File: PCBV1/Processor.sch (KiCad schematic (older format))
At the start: 51 parts, among them SW2 SW_DIP_x02, U1 MCIMX6Y2CVM08AB, Y2 ECS.32712.512, Y3 ECS2401823BJTM

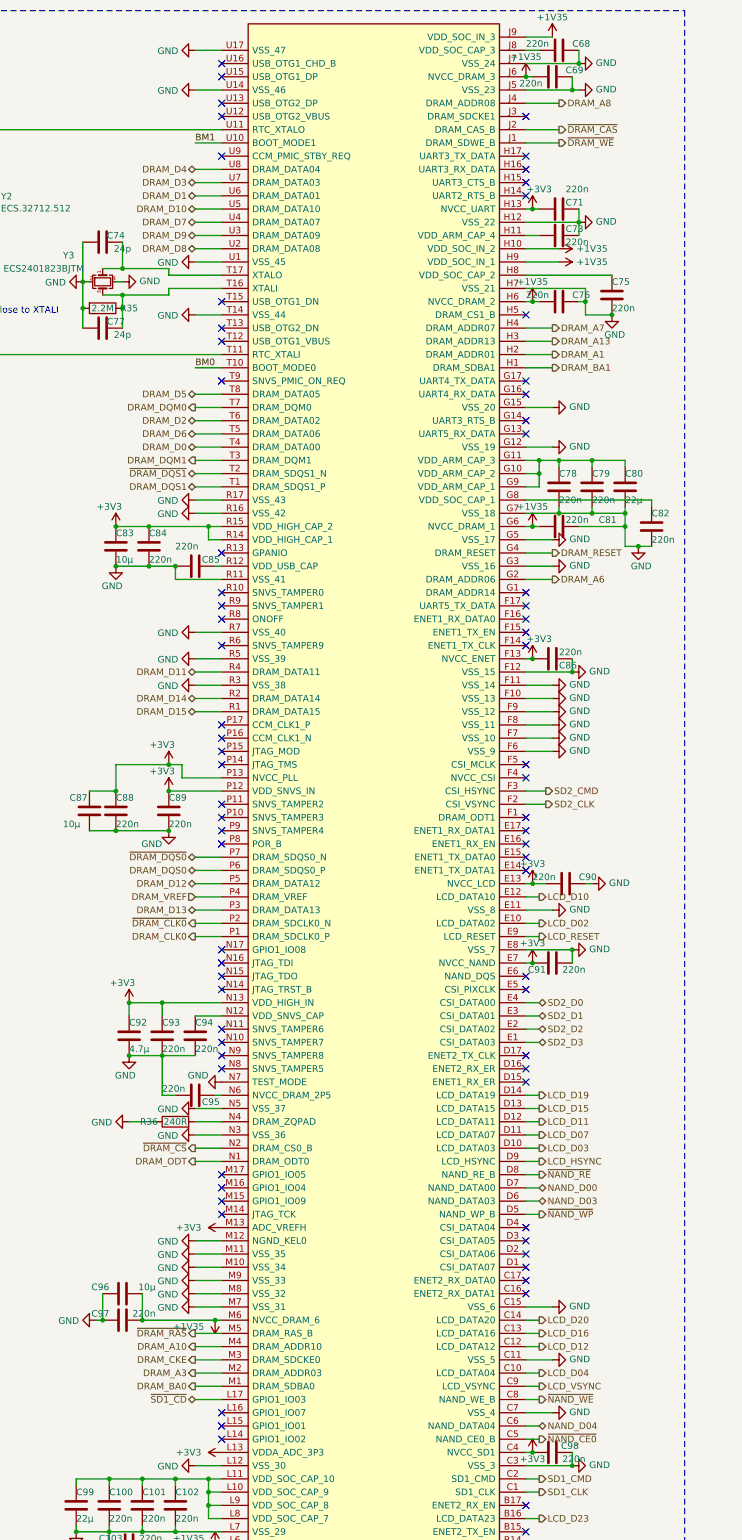
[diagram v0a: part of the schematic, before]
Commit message: Added JTAG, USB OTG, USB Host, and Ethernet.
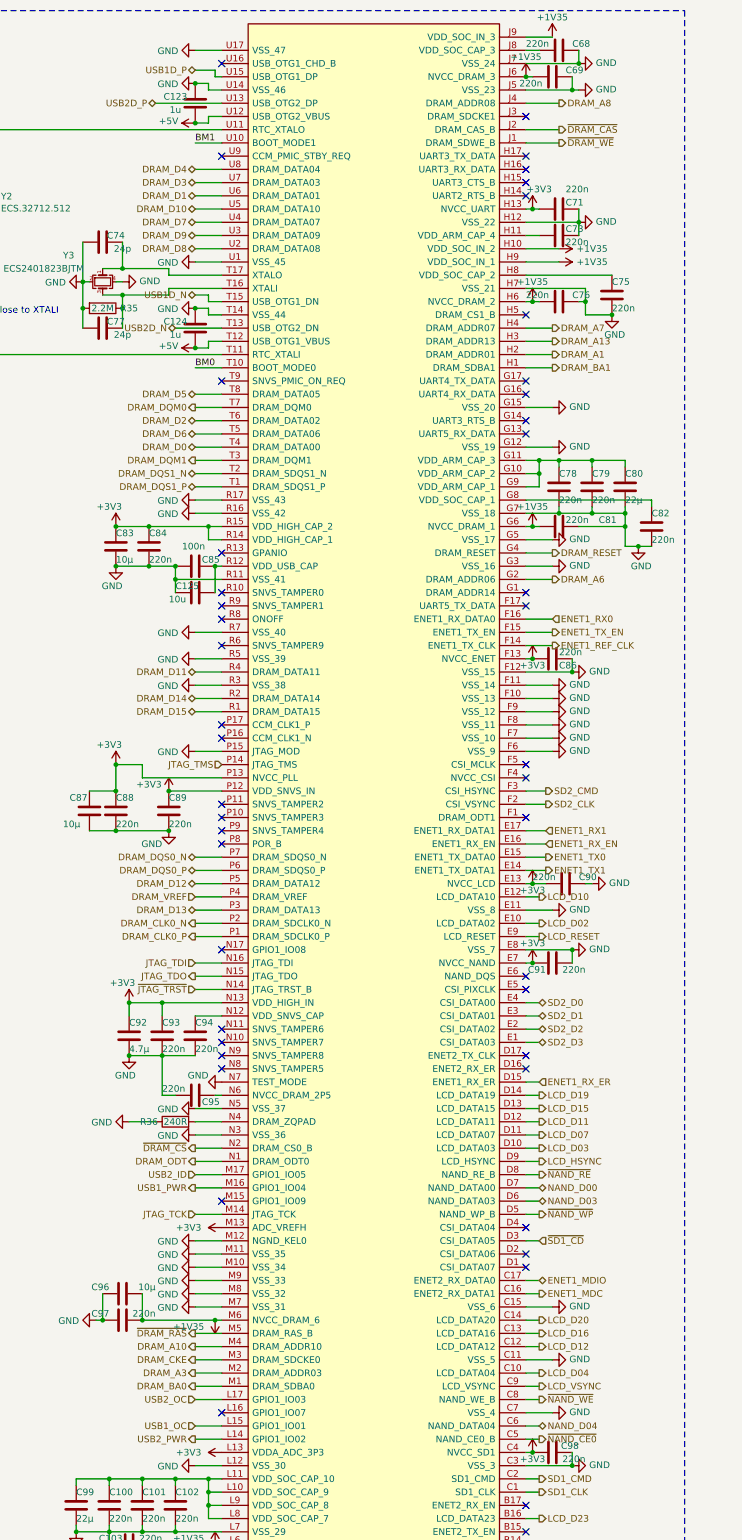
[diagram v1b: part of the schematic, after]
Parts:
- added C123, C124: 1u, Capacitor_SMD:C_0603_1608Metric, symbol Device:C
- added C125: 10u, Capacitor_SMD:C_0402_1005Metric, symbol Device:C
- C85: value 220n -> 100n
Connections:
- net GND: now also U1.P15 (JTAG_MOD), C123.2, C124.2, C125.2
- net ~SD1_CD: now also U1.D3 (CSI_DATA05); no longer U1.L17 (GPIO1_IO03)
- net ENET1_MDC: now reaches U1.C16 (ENET2_RX_DATA1)
- net ENET1_MDIO: now reaches U1.C17 (ENET2_RX_DATA0)
- net ENET1_RX_ER: now reaches U1.D15 (ENET1_RX_ER)
- net ENET1_TX1: now reaches U1.E14 (ENET1_TX_DATA1)
- net ENET1_TX0: now reaches U1.E15 (ENET1_TX_DATA0)
- net ENET1_RX_EN: now reaches U1.E16 (ENET1_RX_EN)
- net ENET1_RX1: now reaches U1.E17 (ENET1_RX_DATA1)
- net ENET1_REF_CLK: now reaches U1.F14 (ENET1_TX_CLK)
- net ENET1_TX_EN: now reaches U1.F15 (ENET1_TX_EN)
- net ENET1_RX0: now reaches U1.F16 (ENET1_RX_DATA0)
- net USB2_PWR: now reaches U1.L14 (GPIO1_IO02)
- net USB1_OC: now reaches U1.L15 (GPIO1_IO01)
- net JTAG_TCK: now reaches U1.M14 (JTAG_TCK)
- net USB1_PWR: now reaches U1.M16 (GPIO1_IO04)
- net USB2_ID: now reaches U1.M17 (GPIO1_IO05)
- net ~JTAG_TRST: now reaches U1.N14 (JTAG_TRST_B)
- net JTAG_TDO: now reaches U1.N15 (JTAG_TDO)
- net JTAG_TDI: now reaches U1.N16 (JTAG_TDI)
- net JTAG_TMS: now reaches U1.P14 (JTAG_TMS)
- net at C85.1, U1.R12 (VDD_USB_CAP): now also C125.1
- net +5V: now reaches U1.T12 (USB_OTG1_VBUS)
- net +5V: now also U1.U12 (USB_OTG2_VBUS), C123.1, C124.1
- net USB2D_N: now reaches U1.T13 (USB_OTG2_DN)
- net USB1D_N: now reaches U1.T15 (USB_OTG1_DN)
- net USB2D_P: now reaches U1.U13 (USB_OTG2_DP)
- net USB1D_P: now reaches U1.U15 (USB_OTG1_DP)
- net DRAM_CLK0 renamed DRAM_CLK0_P
- net DRAM_DQS0 renamed DRAM_DQS0_P
- net DRAM_DQS1 renamed DRAM_DQS1_P
- net ~DRAM_CLK0 renamed DRAM_CLK0_N
- net ~DRAM_DQS0 renamed DRAM_DQS0_N
- net ~DRAM_DQS1 renamed DRAM_DQS1_N
- new net USB2_OC: U1.L17 (GPIO1_IO03)
- no-connect marks 83 -> 56

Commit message: Many changes to footprints (0603 -> 0402), basic DDR layout set, no traces made.
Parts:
- R36: footprint Resistor_SMD:R_0603_1608Metric -> Resistor_SMD:R_0402_1005Metric
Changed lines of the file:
@@
 F 0 "R36" V 2400 9250 50  0000 C CNN
 F 1 "240R" V 2400 9050 50  0000 C CNN
-F 2 "Resistor_SMD:R_0603_1608Metric" V 2330 9050 50  0001 C CNN
+F 2 "Resistor_SMD:R_0402_1005Metric" V 2330 9050 50  0001 C CNN
 F 3 "~" H 2400 9050 50  0001 C CNN
 	1    2400 9050

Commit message: Routing of DDR. Not finished.
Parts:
- removed C108, C68, C73, C75, C82: 220n, Capacitor_SMD:C_0402_1005Metric, symbol Device:C
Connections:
- net ARM_CAP: now reaches C78.1, C79.1, C80.1, U1.G10 (VDD_ARM_CAP_2), U1.G11 (VDD_ARM_CAP_3), U1.G9 (VDD_ARM_CAP_1)
- net ARM_CAP: now also U1.H11 (VDD_ARM_CAP_4)
- net SOC_CAP: now reaches U1.G8 (VDD_SOC_CAP_1)
- net SOC_CAP: now also C100.1, C101.1, C102.1, C99.1, U1.H8 (VDD_SOC_CAP_2), U1.J11 (VDD_SOC_CAP_4), U1.J8 (VDD_SOC_CAP_3), U1.K11 (VDD_SOC_CAP_6), U1.K8 (VDD_SOC_CAP_5), U1.L10 (VDD_SOC_CAP_9), U1.L11 (VDD_SOC_CAP_10), U1.L8 (VDD_SOC_CAP_7), U1.L9 (VDD_SOC_CAP_8)
- no-connect marks 56 -> 54
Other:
- moved on the sheet: R33, R34, SW2
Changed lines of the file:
@@
 L power:GND #PWR0156
 U 1 1 6024A14C
-P 5900 4700
-F 0 "#PWR0156" H 5900 4450 50  0001 C CNN
-F 1 "GND" H 6000 4550 50  0000 R CNN
-F 2 "" H 5900 4700 50  0001 C CNN
-F 3 "" H 5900 4700 50  0001 C CNN
-	1    5900 4700
+P 5800 4550
+F 0 "#PWR0156" H 5800 4300 50  0001 C CNN
+F 1 "GND" H 6050 4450 50  0000 R CNN
+F 2 "" H 5800 4550 50  0001 C CNN
+F 3 "" H 5800 4550 50  0001 C CNN
+	1    5800 4550
 	1    0    0    -1
 $EndComp
@@
 L power:GND #PWR0148
 U 1 1 6024CED6
-P 5700 2950
-F 0 "#PWR0148" H 5700 2700 50  0001 C CNN
-F 1 "GND" H 5800 2800 50  0000 R CNN
-F 2 "" H 5700 2950 50  0001 C CNN
-F 3 "" H 5700 2950 50  0001 C CNN
-	1    5700 2950
-	1    0    0    -1
+P 5500 2850
+F 0 "#PWR0148" H 5500 2600 50  0001 C CNN
+F 1 "GND" V 5500 2700 50  0000 R CNN
+F 2 "" H 5500 2850 50  0001 C CNN
+F 3 "" H 5500 2850 50  0001 C CNN
+	1    5500 2850
+	0    -1   -1   0
 $EndComp
 $Comp
@@
 Connection ~ 2150 13850
 Wire Wire Line
-	2150 13850 2400 13850
-Wire Wire Line
 	1400 13550 1650 13550
 Connection ~ 1400 13550
@@
 U 1 1 6125F3FD
 P 5550 4250
-F 0 "C79" H 5550 4350 50  0000 L CNN
-F 1 "220n" H 5550 4150 50  0000 L CNN
+F 0 "C79" H 5550 4400 50  0000 L CNN
+F 1 "220n" H 5550 4350 50  0000 L CNN
 F 2 "Capacitor_SMD:C_0402_1005Metric" H 5588 4100 50  0001 C CNN
 F 3 "~" H 5550 4250 50  0001 C CNN
@@
 U 1 1 61261154
 P 5300 4250
-F 0 "C78" H 5300 4350 50  0000 L CNN
-F 1 "220n" H 5300 4150 50  0000 L CNN
+F 0 "C78" H 5300 4400 50  0000 L CNN
+F 1 "220n" H 5300 4350 50  0000 L CNN
 F 2 "Capacitor_SMD:C_0402_1005Metric" H 5338 4100 50  0001 C CNN
 F 3 "~" H 5300 4250 50  0001 C CNN
@@
 U 1 1 61261A8E
 P 5800 4250
-F 0 "C80" H 5800 4350 50  0000 L CNN
-F 1 "22µ" H 5800 4150 50  0000 L CNN
+F 0 "C80" H 5800 4400 50  0000 L CNN
+F 1 "22µ" H 5800 4350 50  0000 L CNN
 F 2 "Capacitor_SMD:C_0603_1608Metric" H 5838 4100 50  0001 C CNN
 F 3 "~" H 5800 4250 50  0001 C CNN
@@
 	2200 4850 1950 4850
 Connection ~ 1950 4850
-$Comp
-L Device:C C75
-U 1 1 61402A0D
-P 5700 2800
-F 0 "C75" H 5700 2900 50  0000 L CNN
-F 1 "220n" H 5700 2700 50  0000 L CNN
-F 2 "Capacitor_SMD:C_0402_1005Metric" H 5738 2650 50  0001 C CNN
-F 3 "~" H 5700 2800 50  0001 C CNN
-	1    5700 2800
-	1    0    0    -1
-$EndComp
 Wire Wire Line
 	5500 2750 5500 2850
 Wire Wire Line
-	5500 2950 5700 2950
-Wire Wire Line
 	5050 2750 5500 2750
-Connection ~ 5700 2950
-Wire Wire Line
-	5050 2650 5700 2650
-$Comp
-L Device:C C82
-U 1 1 6141A840
-P 6000 4550
-F 0 "C82" H 6000 4650 50  0000 L CNN
-F 1 "220n" H 6000 4450 50  0000 L CNN
-F 2 "Capacitor_SMD:C_0402_1005Metric" H 6038 4400 50  0001 C CNN
-F 3 "~" H 6000 4550 50  0001 C CNN
-	1    6000 4550
-	1    0    0    -1
-$EndComp
-Wire Wire Line
-	5050 4350 6000 4350
-Wire Wire Line
-	5800 4700 5800 4550
-Connection ~ 5900 4700
-Wire Wire Line
-	5900 4700 5800 4700
-Wire Wire Line
-	6000 4700 5900 4700
-Wire Wire Line
-	6000 4400 6000 4350
 Wire Wire Line
 	2750 6450 2150 6450
@@
 U 1 1 6140FC33
 P 5300 2850
-F 0 "C76" V 5250 2950 50  0000 L CNN
+F 0 "C76" V 5250 2900 50  0000 L CNN
 F 1 "220n" V 5250 2600 50  0000 L CNN
 F 2 "Capacitor_SMD:C_0402_1005Metric" H 5338 2700 50  0001 C CNN
@@
 Wire Wire Line
 	5450 2850 5500 2850
-Connection ~ 5500 2850
-Wire Wire Line
-	5500 2850 5500 2950
 Wire Wire Line
 	5450 4550 5800 4550
-Connection ~ 5800 4550
 Wire Wire Line
 	5800 4550 5800 4450
@@
 	5050 5650 5400 5650
 Connection ~ 5400 5650
-$Comp
-L Device:C C73
-U 1 1 615550B7
-P 5300 2350
-F 0 "C73" V 5250 2400 50  0000 L CNN
-F 1 "220n" V 5350 2400 50  0000 L CNN
-F 2 "Capacitor_SMD:C_0402_1005Metric" H 5338 2200 50  0001 C CNN
-F 3 "~" H 5300 2350 50  0001 C CNN
-	1    5300 2350
-	0    1    1    0
-$EndComp
-Wire Wire Line
-	5050 2350 5150 2350
-Wire Wire Line
-	5450 2350 5450 2250
 Wire Wire Line
 	5050 2250 5450 2250
@@
 Wire Wire Line
 	5450 2150 5450 2250
-$Comp
-L Device:C C68
-U 1 1 6159DBF2
-P 5300 950
-F 0 "C68" V 5250 1050 50  0000 L CNN
-F 1 "220n" V 5250 700 50  0000 L CNN
-F 2 "Capacitor_SMD:C_0402_1005Metric" H 5338 800 50  0001 C CNN
-F 3 "~" H 5300 950 50  0001 C CNN
-	1    5300 950
-	0    1    1    0
-$EndComp
-Wire Wire Line
-	5050 950  5150 950
-Wire Wire Line
-	5450 950  5450 1050
-Connection ~ 5450 1050
 NoConn ~ 2750 4750
 $Comp
@@
 Wire Wire Line
 	5100 4550 5150 4550
-$Comp
-L Device:C C108
-U 1 1 61653ADA
-P 2550 13750
-F 0 "C108" V 2500 13800 50  0000 L CNN
-F 1 "220n" V 2500 13500 50  0000 L CNN
-F 2 "Capacitor_SMD:C_0402_1005Metric" H 2588 13600 50  0001 C CNN
-F 3 "~" H 2550 13750 50  0001 C CNN
-	1    2550 13750
-	0    1    1    0
-$EndComp
-Wire Wire Line
-	2700 13750 2750 13750
-Wire Wire Line
-	2400 13750 2400 13850
-Connection ~ 2400 13850
-Wire Wire Line
-	2400 13850 2750 13850
 $Comp
 L power:+3V3 #PWR0196
@@
 Text Label 2550 1650 0    50   ~ 0
 BM1
-Text Label 8300 1250 0    50   ~ 0
+Text Label 7650 1050 0    50   ~ 0
 BM1
-Text Label 8300 1350 0    50   ~ 0
+Text Label 7650 1150 0    50   ~ 0
 BM0
 $Comp
 L Device:R R34
 U 1 1 6289BF0B
-P 7550 1350
-F 0 "R34" V 7650 1350 50  0000 C CNN
-F 1 "4.7k" V 7550 1350 50  0000 C CNN
-F 2 "Resistor_SMD:R_0603_1608Metric" V 7480 1350 50  0001 C CNN
-F 3 "~" H 7550 1350 50  0001 C CNN
-	1    7550 1350
+P 6900 1150
+F 0 "R34" V 7000 1150 50  0000 C CNN
+F 1 "4.7k" V 6900 1150 50  0000 C CNN
+F 2 "Resistor_SMD:R_0603_1608Metric" V 6830 1150 50  0001 C CNN
+F 3 "~" H 6900 1150 50  0001 C CNN
+	1    6900 1150
 	0    1    1    0
 $EndComp
@@
 L Device:R R33
 U 1 1 6289D793
-P 7550 1250
-F 0 "R33" V 7450 1250 50  0000 C CNN
-F 1 "4.7k" V 7550 1250 50  0000 C CNN
-F 2 "Resistor_SMD:R_0603_1608Metric" V 7480 1250 50  0001 C CNN
-F 3 "~" H 7550 1250 50  0001 C CNN
-	1    7550 1250
+P 6900 1050
+F 0 "R33" V 6800 1050 50  0000 C CNN
+F 1 "4.7k" V 6900 1050 50  0000 C CNN
+F 2 "Resistor_SMD:R_0603_1608Metric" V 6830 1050 50  0001 C CNN
+F 3 "~" H 6900 1050 50  0001 C CNN
+	1    6900 1050
 	0    1    1    0
 $EndComp
@@
 L power:+3V3 #PWR0137
 U 1 1 6289E766
-P 7200 1250
-F 0 "#PWR0137" H 7200 1100 50  0001 C CNN
-F 1 "+3V3" H 7200 1400 50  0000 C CNN
-F 2 "" H 7200 1250 50  0001 C CNN
-F 3 "" H 7200 1250 50  0001 C CNN
-	1    7200 1250
+P 6550 1050
+F 0 "#PWR0137" H 6550 900 50  0001 C CNN
+F 1 "+3V3" H 6550 1200 50  0000 C CNN
+F 2 "" H 6550 1050 50  0001 C CNN
+F 3 "" H 6550 1050 50  0001 C CNN
+	1    6550 1050
 	1    0    0    -1
 $EndComp
 Wire Notes Line
-	7050 1750 8500 1750
+	6400 1550 7850 1550
 Wire Notes Line
-	8500 1750 8500 850
+	7850 1550 7850 650
 Wire Notes Line
-	8500 850  7050 850
+	7850 650  6400 650
 Wire Notes Line
-	7050 850  7050 1750
+	6400 650  6400 1550
 $Comp
 L power:GND #PWR0180
@@
 NoConn ~ 5050 8650
 NoConn ~ 5050 8550
-NoConn ~ 2750 13450
-NoConn ~ 2750 15150
 $Comp
 L power:GND #PWR0185
@@
 NoConn ~ 2750 5050
 NoConn ~ 2750 3450
-Text Notes 7050 1850 0    50   ~ 0
+Text Notes 6400 1650 0    50   ~ 0
 Boot mode switches
-Text Notes 8550 1750 0    50   ~ 0
+Text Notes 7900 1550 0    50   ~ 0
 00: Boot from fuses\n01: Serial downloader\n10: Internal boot\n11: Reserver
 $Comp
 L Switch:SW_DIP_x02 SW2
 U 1 1 62DA78FC
-P 8000 1350
-F 0 "SW2" H 8000 1717 50  0000 C CNN
-F 1 "SW_DIP_x02" H 8000 1626 50  0000 C CNN
-F 2 "Button_Switch_SMD:SW_DIP_SPSTx02_Slide_6.7x6.64mm_W6.73mm_P2.54mm_LowProfile_JPin" H 8000 1350 50  0001 C CNN
-F 3 "https://www.mouser.dk/datasheet/2/96/219-1144706.pdf" H 8000 1350 50  0001 C CNN
-	1    8000 1350
-	1    0    0    -1
-$EndComp
-Wire Wire Line
-	7200 1250 7400 1250
-Wire Wire Line
-	7400 1250 7400 1350
-Connection ~ 7400 1250
+P 7350 1150
+F 0 "SW2" H 7350 1517 50  0000 C CNN
+F 1 "SW_DIP_x02" H 7350 1426 50  0000 C CNN
+F 2 "Button_Switch_SMD:SW_DIP_SPSTx02_Slide_6.7x6.64mm_W6.73mm_P2.54mm_LowProfile_JPin" H 7350 1150 50  0001 C CNN
+F 3 "https://www.mouser.dk/datasheet/2/96/219-1144706.pdf" H 7350 1150 50  0001 C CNN
+	1    7350 1150
+	1    0    0    -1
+$EndComp
+Wire Wire Line
+	6550 1050 6750 1050
+Wire Wire Line
+	6750 1050 6750 1150
+Connection ~ 6750 1050
 Wire Wire Line
 	5050 6550 5200 6550
@@
 U 1 1 62CB2A64
 P 2550 5050
-F 0 "C125" V 2500 4900 50  0000 L CNN
+F 0 "C125" V 2500 4800 50  0000 L CNN
 F 1 "10u" V 2600 4850 50  0000 L CNN
 F 2 "Capacitor_SMD:C_0402_1005Metric" H 2588 4900 50  0001 C CNN
@@
 Wire Wire Line
 	5200 6950 5050 6950
+Text Label 1650 11750 0    50   ~ 0
+SOC_CAP
+Text Label 2400 13450 0    50   ~ 0
+SOC_CAP
+Wire Wire Line
+	2400 13450 2750 13450
+Wire Wire Line
+	2150 13850 2750 13850
+Text Label 2400 13750 0    50   ~ 0
+SOC_CAP
+Wire Wire Line
+	2400 13750 2750 13750
+Text Label 2400 15150 0    50   ~ 0
+SOC_CAP
+Wire Wire Line
+	2750 15150 2400 15150
+Text Label 5400 950  2    50   ~ 0
+SOC_CAP
+Wire Wire Line
+	5050 950  5400 950
+Text Label 5400 2650 2    50   ~ 0
+SOC_CAP
+Connection ~ 5500 2850
+Wire Wire Line
+	5400 2650 5050 2650
+Text Label 5400 4350 2    50   ~ 0
+SOC_CAP
+Connection ~ 5800 4550
+Wire Wire Line
+	5400 4350 5050 4350
+Text Label 5400 2350 2    50   ~ 0
+ARM_CAP
+Wire Wire Line
+	5050 2350 5400 2350
+Text Label 5550 4050 0    50   ~ 0
+ARM_CAP
 $EndSCHEMATC
